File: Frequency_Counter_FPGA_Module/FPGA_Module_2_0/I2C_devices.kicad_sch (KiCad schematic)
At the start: 45 parts, among them J14 PLL2_CLK2, J15 PLL2_CLK1, U4 SI5356A, U5 ADS1115, U6 TMP117xxDRV, U8 TMP117xxDRV

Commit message: feat(boot): LED selftest blikaci kod + RTC LSE medium-low drive; UI 4.3" audit; FPGA HW revize
STM32H757 firmware:
- bootled.c/h: boot-time HW selftest diagnostika na LED_1 (PG3). Kazdy
  sledovany periferni init (FMC/SPI2/I2C4/DSIHOST/LTDC/USART1/RTC/ADC3/
  QUADSPI/I2C1) + display bring-up (panel probe/power-on/DSI start/
  TC358762) si zaznamena poradove cislo; pri zaseknuti v Error_Handler()
  LED bez displeje zabliká N-krat podle poradi. Regen-safe (jen chranene
  USER CODE hooky), bez zpozdeni v happy-path.
- RTC LSE Drive Capability LOW -> MEDIUM LOW (H757_LED.ioc): kompenzuje
  desky s predimenzovanymi zatezovymi kondenzatory krystalu (22pF misto
  18pF), ktere LSE nerozjizdely.
- UI audit pro realny 4,3" 800x480 panel (8,54 px/mm): hit-slop pilulek,
  fonty, HDR_PILL_LIMIT fit-check, Menu 3x4 mrizka s placeholdery, oprava
  ghost bugu AUTO CET/CEST tlacitka, sign-loss bug ve fmt_fixed/fmt_minmax.
  main-old layout zamrazen jako default (A/B srovnani, viz STATUS.md #14).

FPGA carrier v2.0 (KiCad): prubezne review checklisty a schema/PCB revize.

Co-Authored-By: OK2JNJ <ok2jnj@local>
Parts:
- removed R107, R110: 33R, Resistor_SMD:R_0805_2012Metric, symbol Device:R
- added C53, C54, C55: 100n, Capacitor_SMD:C_0805_2012Metric, symbol Device:C_Small
- added C56: 10n, Capacitor_SMD:C_0805_2012Metric, symbol Device:C_Small
- added U12: AD5693RxRM, Package_SO:MSOP-10_3x3mm_P0.5mm, symbol Analog_DAC:AD5693RxRM
- J6: renamed from J14; value PLL2_CLK2 -> CLK_OUT_1
- J7: renamed from J15; value PLL2_CLK1 -> CLK_OUT_2
- renumbered C27 to C37, C28 to C38, C29 to C39, C33 to C40, C34 to C41, C30 to C42, C31 to C43, C32 to C44, C114 to C45, C35 to C46, C36 to C47, C37 to C48, C38 to C49, C45 to C50, C4 to C51, C5 to C52, R96 to R51, R92 to R52, R89 to R53, R90 to R54, R97 to R55, R98 to R56, R37 to R57, R38 to R58, R39 to R59, R40 to R60, R41 to R61, R42 to R62, R43 to R63, R44 to R64, R45 to R65, R35 to R66, R36 to R67, R52 to R68, R53 to R69, R71 to R70, R72 to R71, U6 to U10, U8 to U11, U5 to U8, U4 to U9
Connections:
- net PLL2_CLK1 is gone; now on net CLK_OUT_2: R71.1
- net PLL2_CLK2 is gone; now on net CLK_OUT_1: R70.1
- net +3V3: now also C53.2, U12.2 (VLOGIC), U12.3 (~{RESET})
- net +5V: now also C54.1, U12.1 (VDD)
- net GND: now also C53.1, C54.2, C55.1, C56.1, U12.4 (~{LDAC}), U12.5 (GND), U12.6 (A0)
- net OCXO_VC: now also C56.2, U12.10 (VOUT); no longer R51.2
- net PLL_CLK4: now also R69.1; no longer R69.2
- net SCL: now also U12.7 (SCL)
- net SDA: now also U12.8 (SDA)
- net CLK_OUT_2: now reaches U9.9 (CLK_7)
- net CLK_OUT_1: now reaches U9.13 (CLK_5)
- net at U9.10 (CLK_6): now also R69.2; no longer R69.1
- net 10MHz_GPSDO_CLK3 renamed 10MHz_GPSDO_CLK1
- new net: C55.2, U12.9 (VREF)
- new net OCXO_VC_Sense: R51.2
- no-connect marks 2 -> 4
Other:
- note added: "Addr: 0x4C"
- note added: "Zmensit? v ceste 2x"
- moved on the sheet: C42, C43, C44, C45, C46, C47, C48, C49, C50, C51, C52, J6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

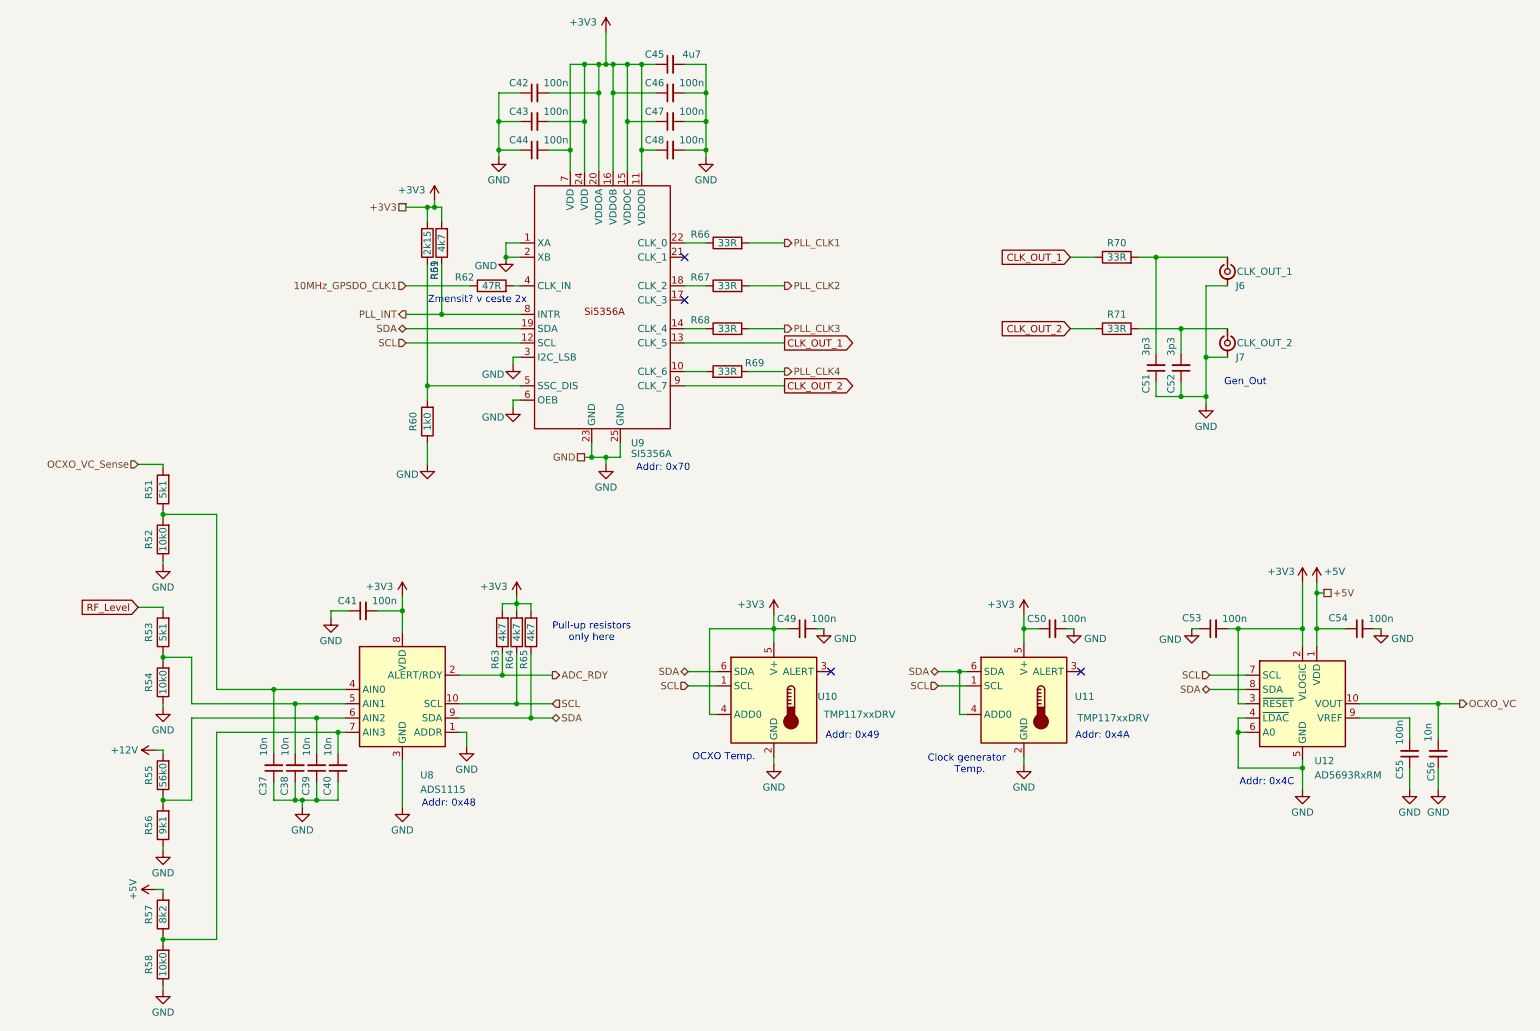
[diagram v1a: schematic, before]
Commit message: feat(hw): FPGA carrier v2.0 — aktualizace schematu + PCB + checklist
KiCad FPGA_Module_2_0 (FPGA_Core/GPSDO/I2C_devices/power_supply schemata,
PCB layout, project), BOARD_V20_CHECKLIST.md. Odstranen zastaraly
FPGA_module_schematic.pdf (nahrazen exportem FPGA_module.pdf).

Co-Authored-By: OK2JNJ <ok2jnj@users.noreply.github.com>
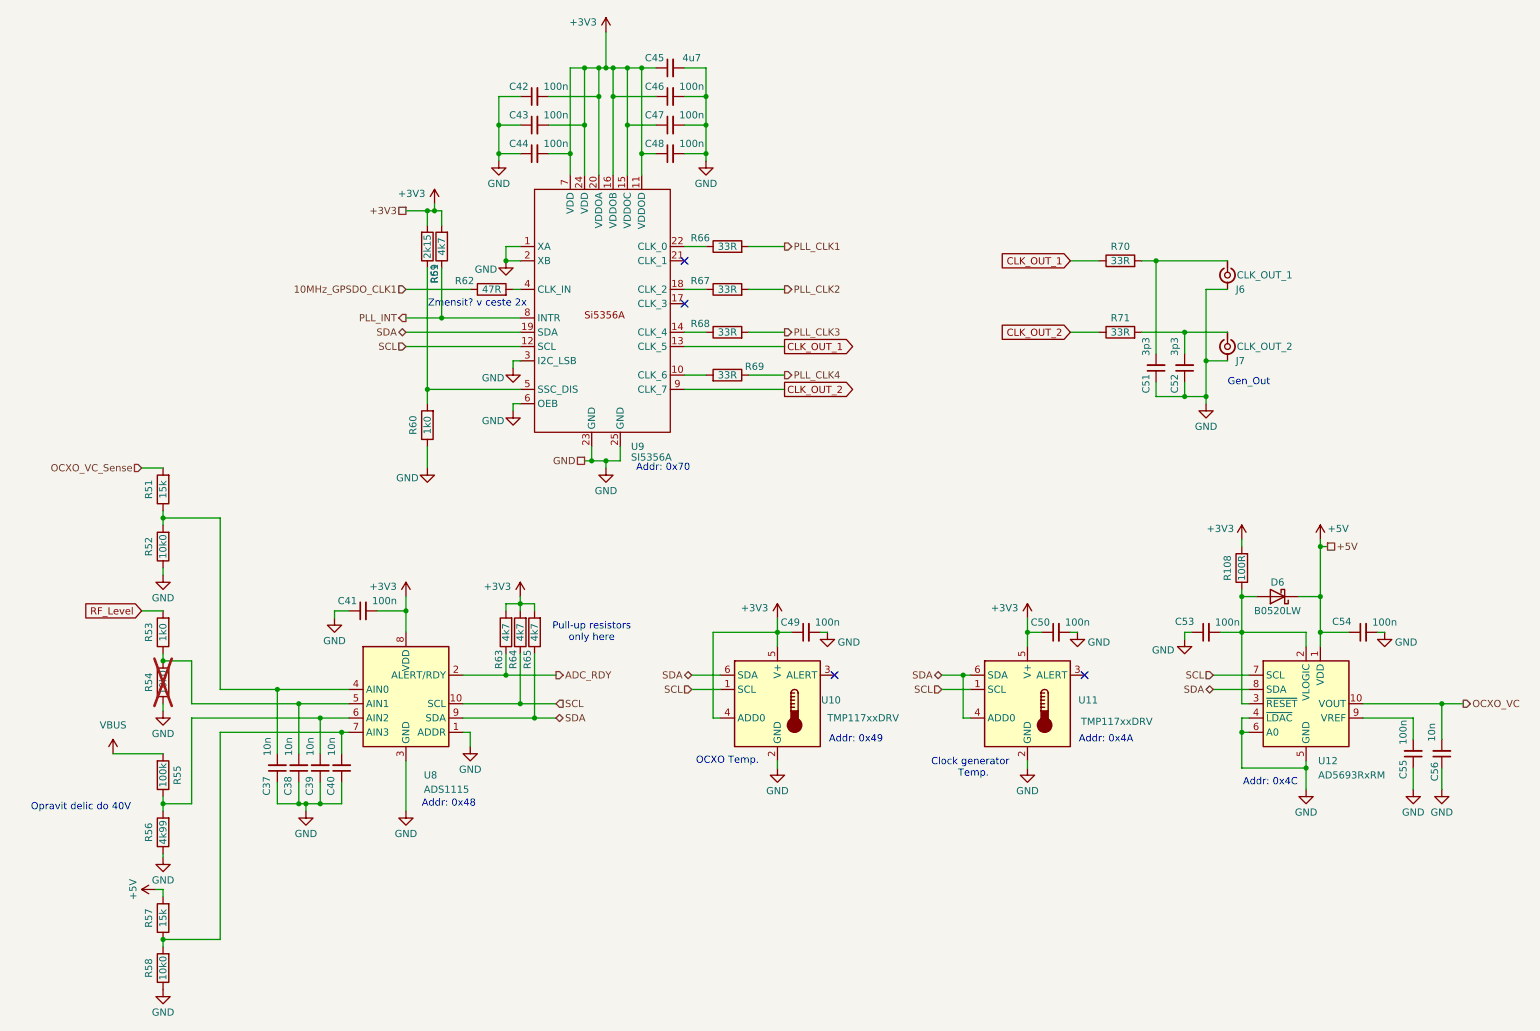
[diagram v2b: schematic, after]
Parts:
- added D6: B0520LW, Diode_SMD:D_SOD-123, symbol Device:D_Schottky
- added R108: 100R, Resistor_SMD:R_0805_2012Metric, symbol Device:R
- R51: value 5k1 -> 15k
- R53: value 5k1 -> 1k0
- R54: now not fitted
- R55: value 56k0 -> 100k
- R56: value 9k1 -> 4k99
- R57: value 8k2 -> 15k
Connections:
- net +3V3: now also R108.2; no longer C53.2, U12.2 (VLOGIC), U12.3 (~{RESET})
- net +5V: now also D6.1 (K)
- net +12V renamed VBUS
- new net: C53.2, D6.2 (A), R108.1, U12.2 (VLOGIC), U12.3 (~{RESET})
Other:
- note added: "Opravit delic do 40V"
- moved on the sheet: C37, C38, C39, C40, C42, C43, C44, C45, C46, C47, C48, C49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
